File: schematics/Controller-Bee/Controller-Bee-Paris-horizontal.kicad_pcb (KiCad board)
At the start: 2 copper layers, 22.8 x 60.5 mm, 21 parts, among them P1 CONN_01X05, P2 CONN_02X04, P3 USB_OTG, P4 CONN_02X04, U1 EFM8UB10F8G-B-QFN20

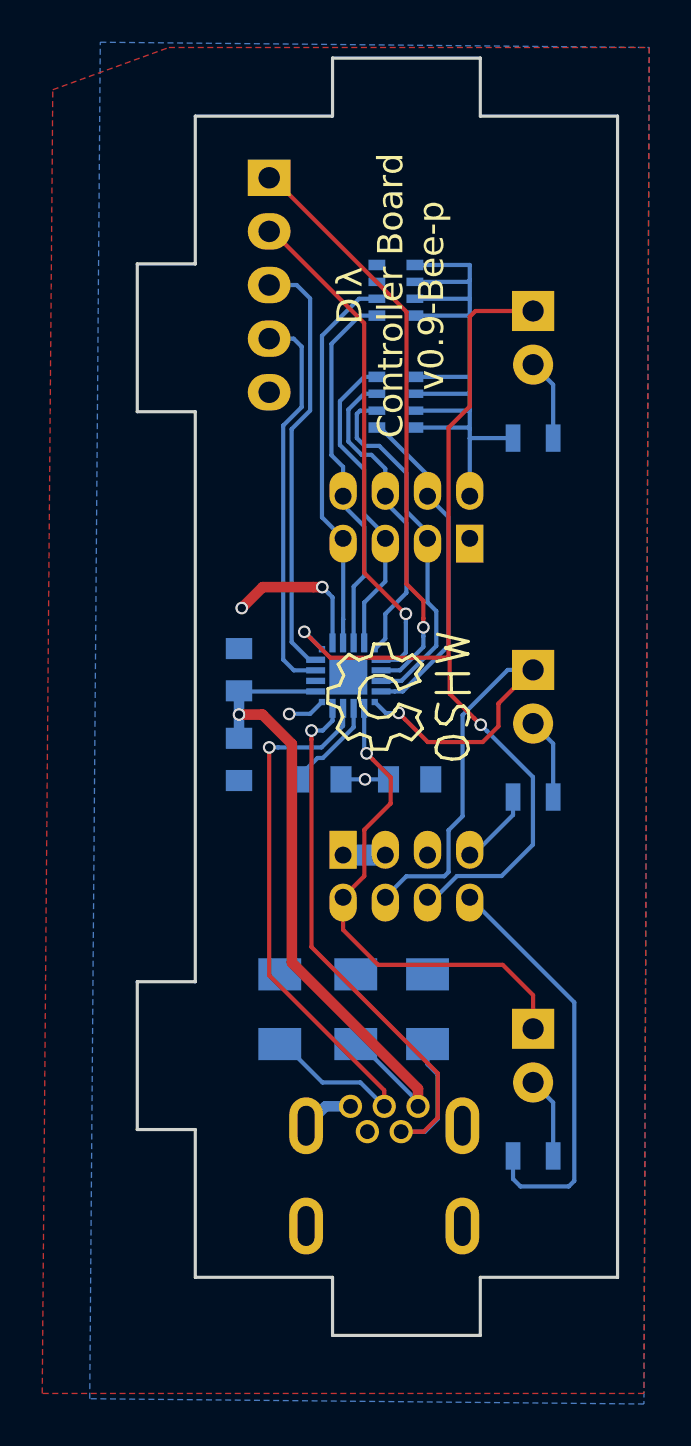
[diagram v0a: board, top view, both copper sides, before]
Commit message: schematics: update LED connections, use 4x resistor arrays
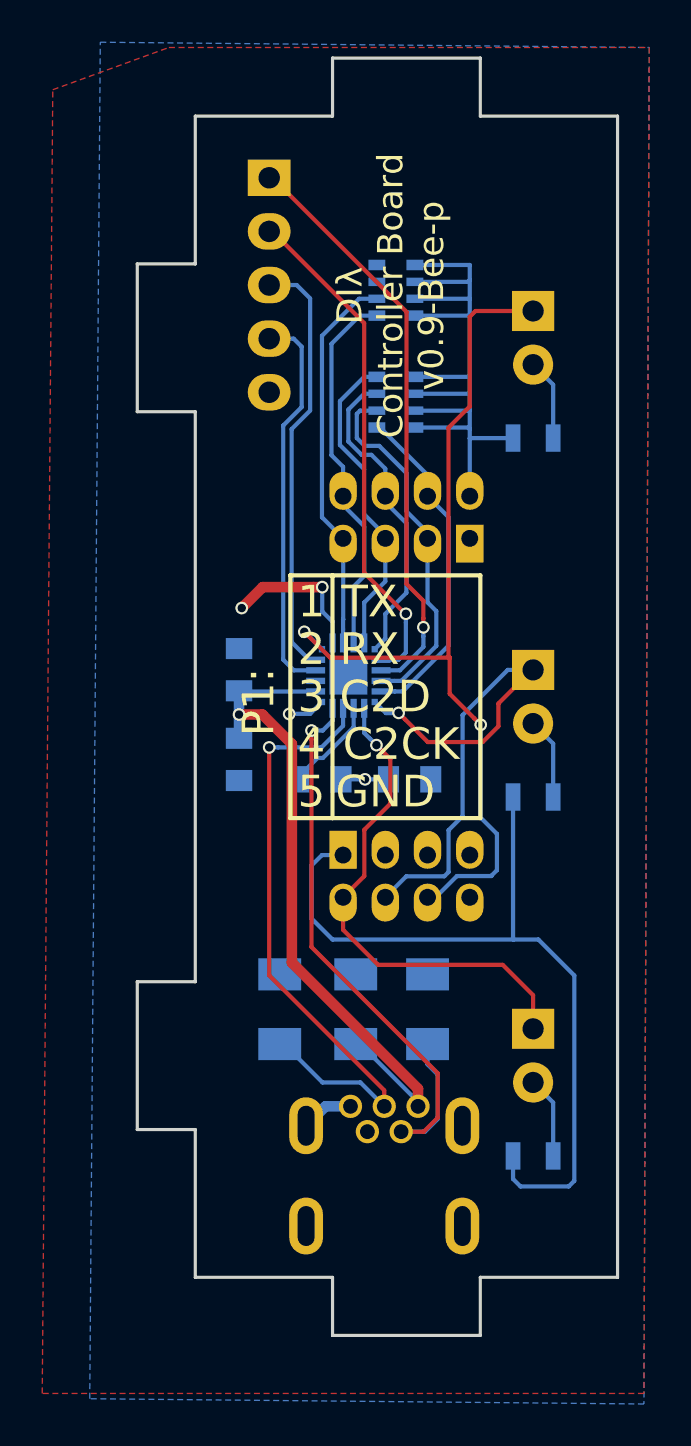
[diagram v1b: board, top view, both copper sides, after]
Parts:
- removed D4, D5, D6: LED, LEDs:LED-5MM
- removed REF**: Symbol_OSHW-Logo_SilkScreen, Symbols:Symbol_OSHW-Logo_SilkScreen
- added LED1: LED, LEDs:LED-5MM, B.Cu at (201.0, 113.2)
- added LED2: LED, LEDs:LED-5MM, B.Cu at (201.0, 96.2)
- added LED3: LED, LEDs:LED-5MM, B.Cu at (201.0, 79.2)
- R1, R2, R3: value R -> 220
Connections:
- P3 pad 4: Net-(P3-Pad4) -> (no net)
- P4 pad 3: VDD -> (no net)
- P4 pad 5: VDD -> (no net)
- P4 pad 7: VDD -> (no net)
- P4 pad 8: VDD -> (no net)
- RP2 pad 3: Net-(RP2-Pad3) -> (no net)
- RP2 pad 4: Net-(RP2-Pad4) -> (no net)
- U1 pad 0: Net-(U1-Pad0) -> (no net)
- U1 pad 8: Net-(U1-Pad8) -> (no net)
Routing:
- net VDD: track 63.5 -> 76.5 mm
- net iLED3: track 43.8 -> 42.1 mm
- net iLED2: track 26.8 -> 25.8 mm
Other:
- board text added: "2"
- board text added: "3"
- board text added: "4"
- board text added: "5"
- board text added: "C2CK"
- board text added: "C2D"
- board text added: "GND"
- board text added: "P1:"
- board text added: "RX"
- board text added: "TX"

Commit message: Schematics update
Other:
- board text added: "DIλ Controller board v0.9-Bee-p-h"
- board text removed: "DIλ Controller Board v0.9-Bee-p"
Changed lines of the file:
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@@
     (links 63)
     (no_connects 0)
-    (area 182.174999 67.174999 205.075001 127.825001)
+    (area 150.000001 47.15 210.160715 157.700001)
     (thickness 1.6)
-    (drawings 65)
+    (drawings 67)
     (tracks 274)
     (zones 0)
@@
     (visible_elements FFFFFF7F)
     (pcbplotparams
-      (layerselection 0x00030_80000001)
-      (usegerberextensions false)
+      (layerselection 0x010f0_80000001)
+      (usegerberextensions true)
       (excludeedgelayer true)
       (linewidth 0.100000)
@@
       (viasonmask false)
       (mode 1)
-      (useauxorigin false)
+      (useauxorigin true)
       (hpglpennumber 1)
       (hpglpenspeed 20)
@@
       (plotvalue true)
       (plotinvisibletext false)
-      (padsonsilk false)
+      (padsonsilk true)
       (subtractmaskfromsilk false)
       (outputformat 1)
       (mirror false)
-      (drillshape 1)
+      (drillshape 0)
       (scaleselection 1)
-      (outputdirectory ""))
+      (outputdirectory Controller-Bee-Paris-horizontal))
   )
   (net 0 "")
@@
     )
   )
+  (gr_text 1 (at 192 103 90) (layer B.SilkS)
+    (effects (font (size 1.5 1.5) (thickness 0.3)) (justify mirror))
+  )
+  (gr_text 1 (at 198.25 92.5 90) (layer B.SilkS)
+    (effects (font (size 1.5 1.5) (thickness 0.3)) (justify mirror))
+  )
   (gr_text P1: (at 188 97.75 90) (layer F.SilkS)
     (effects (font (size 1.5 1.5) (thickness 0.3)))
@@
     (effects (font (size 1.5 1.5) (thickness 0.3)))
   )
-  (gr_text "DIλ\nController Board\nv0.9-Bee-p" (at 194.25 78.5 90) (layer F.SilkS)
+  (gr_text "DIλ\nController board\nv0.9-Bee-p-h" (at 194.25 78.5 90) (layer F.SilkS)
     (effects (font (size 1.2 1.2) (thickness 0.25)))
   )
